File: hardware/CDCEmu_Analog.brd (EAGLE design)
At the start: 60 x 40 mm, 63 parts, among them J1 Audio In, J2 Audio Out, J3 Mic In, Q1 PCH, Q2 NCH, Q3 NCH, Q4 PCH, Q5 NCH, Q6 NPN, Q7 NPN, Q8 NPN, Q9 NPN, U1 1117, U2 BK8000L, U3 NE5532D

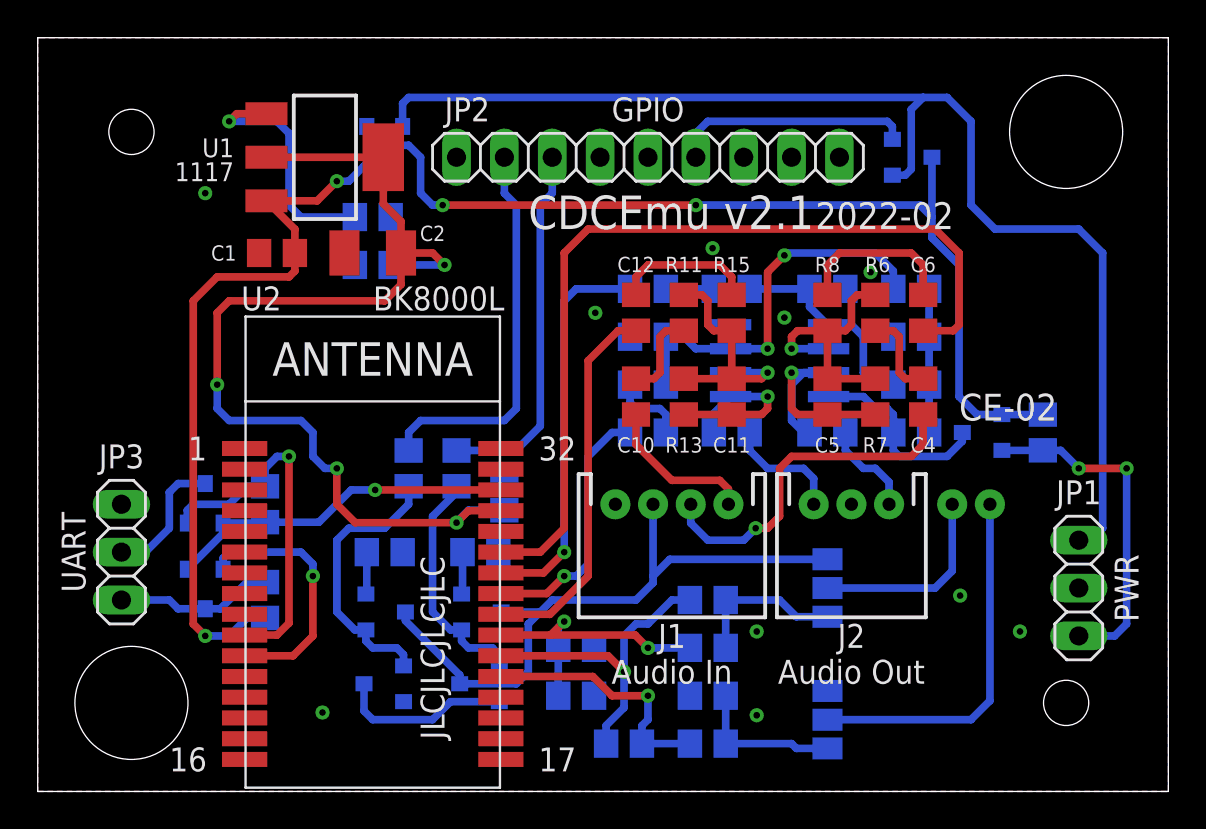
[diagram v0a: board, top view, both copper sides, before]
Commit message: [HW] Add audio gain control trimpots
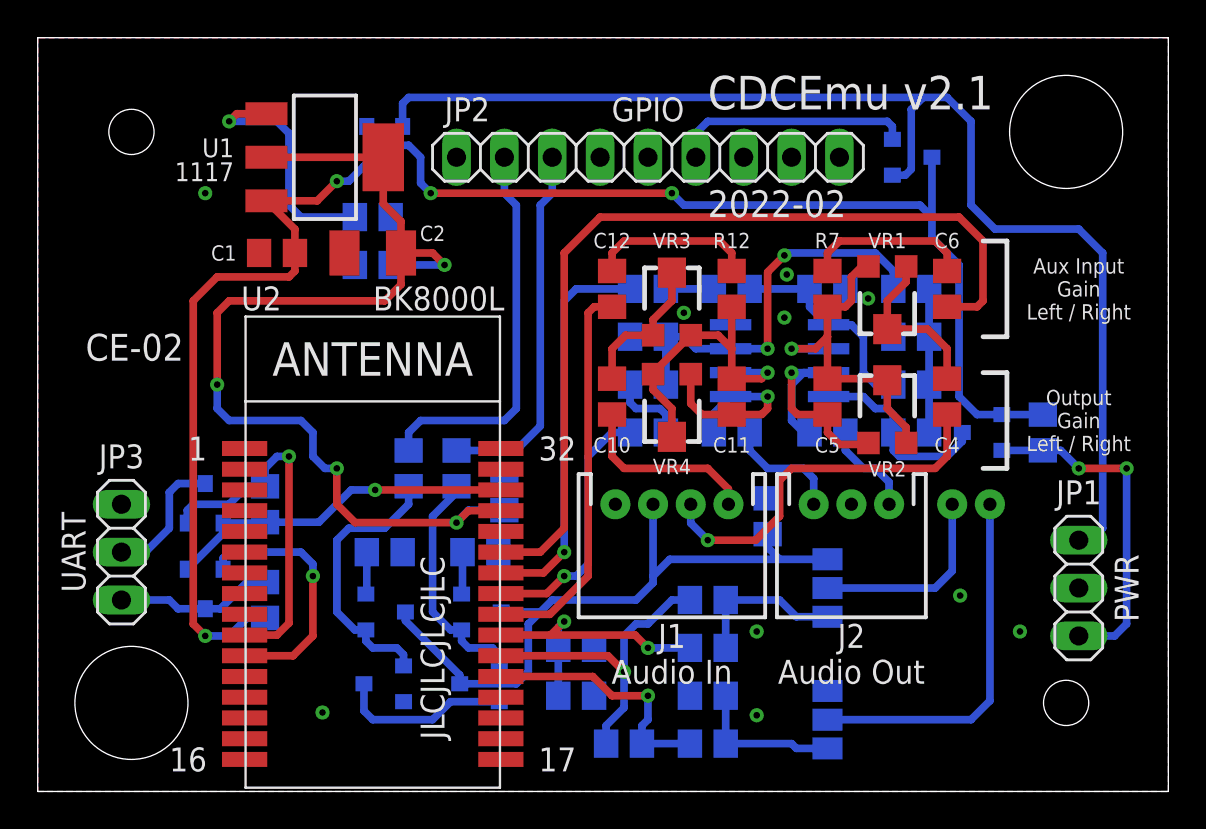
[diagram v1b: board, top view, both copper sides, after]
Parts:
- removed C16: 1u, rcl:C0805
- removed R21: 1k, rcl:R0805
- removed R22, R23: 1.2k, rcl:R0805
- added C21: 1u, rcl:C0805
- added VR1, VR2, VR3, VR4: 10k, SparkFun-Resistors:TRIMPOT-SMD-TC33X
- C17: value 10n -> 1u
- C18: value 1u -> 10n
- C19: value 100n -> 1u
- C20: value 1u -> 100n
- R10: value 1k -> 10k
- R18, R9: value 10k -> 1k
- R19, R20: value 10k -> 1.2k
- R6: value 10k -> 100k
- moved R18 31.2 mm to (46.4, 26.7)
- moved R17 25.6 mm to (46.4, 24.1), turned to 180 degrees
- moved R10 24.5 mm to (22.2, 17.1), turned to 270 degrees
- moved R14 23.7 mm to (23.5, 12.7)
- moved R15 22.4 mm to (18.4, 12.7), flipped to the bottom, turned to 0 degrees
- moved R20 21.9 mm to (35.6, 5.08)
- moved R12 17.4 mm to (36.8, 26.7), flipped to the top
- moved R13 15.1 mm to (19.7, 17.1), flipped to the bottom
- moved R19 14.3 mm to (35.6, 7.62)
- moved R11 13.6 mm to (46.4, 19.1), flipped to the bottom, turned to 0 degrees
- moved R16 13.5 mm to (32.4, 21.6), turned to 180 degrees
- moved R6 12.2 mm to (38.7, 14.6), flipped to the bottom, turned to 270 degrees
- moved R9 10.8 mm to (46.4, 21.6), turned to 0 degrees
- moved C17 8.82 mm to (35.6, 10.2)
- moved C19 7.43 mm to (35.6, 2.54)
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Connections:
- net +12V: now also R11.2; no longer R14.2
- net AGND: now also R11.1, R17.2, R18.1, R9.1; no longer R10.1, R14.1, R20.2, R21.1
- net BT_MICN: now also C19.2, R20.2; no longer C18.2, R23.2
- net BT_MICP: now also C17.2, R19.2; no longer C16.2, R22.2
- net CTRL: now also R6.2
- net GND: now also C21.2, R14.1, R15.1, R6.1; no longer C19.2, R18.1, R23.1
- net L+: now also R16.2, R18.2; no longer R19.2, R21.2
- net L-: now also R12.2, VR3.3, VR4.2, VR4.3; no longer R11.2, R13.1, R15.2
- net L1: now also VR3.1, VR3.2; no longer R11.1
- net L2: now also R12.1; no longer R15.1
- net L3: now also R16.1; no longer R19.1
- net LOUT: now also VR4.1; no longer R13.2
- net MIC_N: now also C18.2, C19.1; no longer C17.2, C18.1
- net MIC_P: now also C18.1; no longer C16.1
- net P3: now also R10.1; no longer R12.1
- net P3B: now also R10.2; no longer R12.2
- net P7: now also R13.1; no longer R16.1
- net P7B: now also R13.2; no longer R16.2
- net Q7E: now also R14.2; no longer R17.2
- net Q8E: now also R15.2; no longer R18.2
- net R+: now also R8.2; no longer R10.2
- net R-: now also R7.2, VR1.3, VR2.2, VR2.3; no longer R6.2, R7.1, R8.2
- net R1: now also VR1.1, VR1.2; no longer R6.1
- net R2: now also R7.1; no longer R8.1
- net R3: now also R8.1; no longer R9.1
- net ROUT: now also VR2.1; no longer R7.2
- net VMIC: now also C21.1, R19.1; no longer C19.1, R22.1
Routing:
- net R-: track 13.8 -> 18.7 mm
- net R1: track 4.71 -> 8.93 mm
- net L-: track 13.2 -> 16.9 mm
- net L1: track 4.71 -> 7.80 mm
- net AUX_L: track 8.28 -> 9.93 mm
- net CTRL: track 34.8 -> 36.4 mm
- net LOUT: track 9.45 -> 10.9 mm
- net L2: track 7.52 -> 8.79 mm
- net AUX_R: track 18.9 -> 20.2 mm
- net BT_RN: track 46.3 -> 47.2 mm
- net ROUT: track 13.8 -> 14.7 mm
- net BT_LN: track 20.1 -> 20.8 mm
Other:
- board text added: "Aux Input Gain Left / Right"
- board text added: "Mic Input Target"
- board text added: "Output Gain Left / Right"

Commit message: [HW/Analog] Add audio signal detection
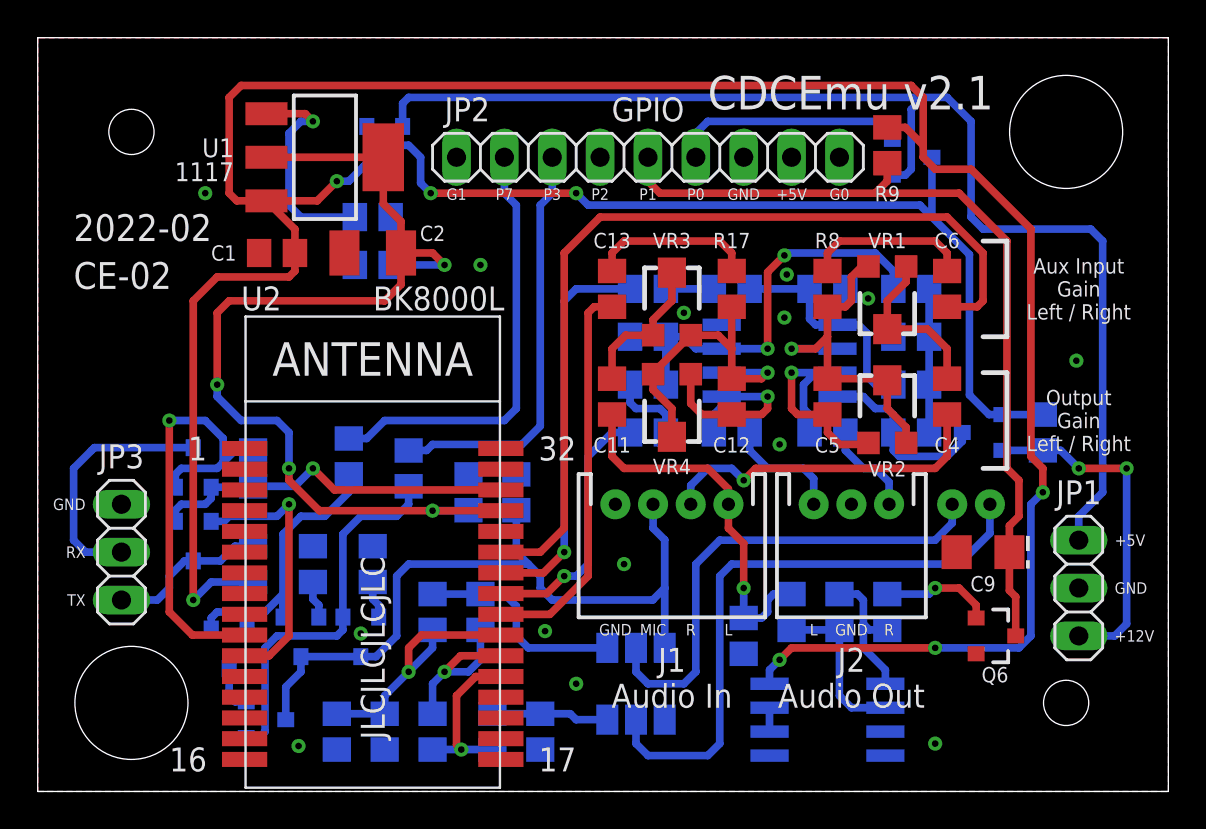
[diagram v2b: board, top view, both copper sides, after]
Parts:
- added C16: 47p, rcl:C0805
- added Q10: NPN, SparkFun-DiscreteSemi:SOT23-3
- added R21, R22: 10k, rcl:R0805
- added R23: 1k, rcl:R0805
- added R24, R25: 1.2k, rcl:R0805
- added U4: NE5532, custom:SO08
- C10, C12: value 1u -> 47p
- C11, C15: value 47p -> 1u
- C9: value 47p -> 10u; device rcl:C0805 -> custom:C1206-POL
- R11: value 10k -> 220
- R13: value 10k -> 1k
- R18: value 1k -> 10k
- R19, R20: value 1.2k -> 10k
- R6: value 100k -> 10k
- R7: value 10k -> 100k
- R9: value 1k -> 100k
- U3: value NE5532D -> LM358; device linear:SO08 -> custom:SO08
- moved R18 31.1 mm to (16.5, 17.8), turned to 270 degrees
- moved Q6 27.4 mm to (50.8, 8.26), flipped to the top
- moved R13 27.0 mm to (46.4, 21.6), turned to 0 degrees
- moved R20 22.1 mm to (14.6, 12.1), turned to 270 degrees
- moved R7 19.7 mm to (25.4, 15.9), flipped to the bottom
- moved U3 19.2 mm to (41.9, 3.81), turned to 270 degrees
- moved R12 19.0 mm to (45.1, 9.53), flipped to the bottom, turned to 90 degrees
- moved R19 18.3 mm to (17.8, 12.1), turned to 270 degrees
- moved R10 17.4 mm to (36.8, 26.7), turned to 180 degrees
- moved C9 16.2 mm to (50.2, 12.7), flipped to the top, turned to 180 degrees
- moved R14 14.7 mm to (37.5, 8.26), turned to 90 degrees
- moved R16 14.2 mm to (46.4, 19.1), turned to 0 degrees
- moved C21 13.5 mm to (15.9, 3.17), turned to 270 degrees
- moved Q7 12.8 mm to (12.1, 3.81)
- moved C10 12.8 mm to (41.9, 26.7), flipped to the bottom, turned to 0 degrees
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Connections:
- new net DET-: R11.2, R6.1, U3.2
- new net DETOUT: R12.1, R6.2, U3.1
- new net DET_B: Q6.1, R12.2
- new net U4FB: U3.6, U3.7
- net +12V: now also R16.2, U4.8; no longer R11.2, U3.8
- net +5V: now also R9.2, U3.8
- net AGND: now also R13.1, R16.1, R22.2, R23.1; no longer R11.1, R17.2, R18.1, R9.1
- net AUX_L: now also C11.1, R11.1, R14.2; no longer C10.1
- net BT_LN: now also C13.1; no longer C12.1
- net BT_LP: now also C15.1; no longer C14.1
- net BT_MICN: now also R25.2, SJ1.1; no longer R20.2, SJ1.3
- net BT_MICP: now also R24.2, SJ2.1; no longer R19.2, SJ2.3
- net CCE: now also Q10.3, Q7.2; no longer Q6.2, Q9.3
- net CTRL: now also Q9.3, R7.2, SJ2.3; no longer Q6.3, R6.2, SJ2.1
- net GND: now also C10.1, C16.1, C9.2, Q10.2, Q6.2, R19.1, R22.1, R25.1, R7.1, SJ1.3, U3.3, U3.5, U4.4; no longer C15.1, C9.1, Q9.2, R15.1, R17.1, R6.1, SJ1.1
- net L: now also C14.2; no longer C13.2
- net L+: now also C16.2, R21.2, R23.2, U4.3; no longer C15.2, R16.2, R18.2, U3.3
- net L-: now also C12.1, R17.2, U4.2; no longer C11.1, R12.2, U3.2
- net L1: now also C11.2; no longer C10.2
- net L2: now also C13.2, R17.1; no longer C12.2, R12.1
- net L3: now also C15.2, R21.1; no longer C14.2, R16.1
- net LOUT: now also C12.2, C14.1, U4.1; no longer C11.2, C13.1, U3.1
- net P1: now also C9.1, Q6.3, R9.1
- net P3: now also R15.1; no longer R10.1
- net P3B: now also Q8.1, R15.2; no longer Q6.1, R10.2
- net P7: now also R18.1; no longer R13.1
- net P7B: now also Q10.1, R18.2; no longer Q8.1, R13.2
- net Q7E: now also Q8.2, R19.2; no longer Q7.2, R14.2
- net Q8E: now also Q9.2, R20.2; no longer Q8.2, R15.2
- net R+: now also C10.2, R10.2, R13.2, U4.5; no longer C9.2, R8.2, R9.2, U3.5
- net R-: now also R8.2, U4.6; no longer R7.2, U3.6
- net R2: now also R8.1; no longer R7.1
- net R3: now also R10.1; no longer R8.1
- net ROUT: now also U4.7; no longer U3.7
- net VMIC: now also R24.1; no longer R19.1
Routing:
- net +5V: track 39.1 -> 131.7 mm, vias 2 -> 5
- net P1: track 0.00 -> 45.1 mm
- net MIC: track 10.5 -> 26.2 mm
- net MICGND: track 19.5 -> 31.9 mm
- net AUX_L: track 9.93 -> 19.7 mm, vias 0 -> 1
- net DET-: track 0.00 -> 8.74 mm
- net DETOUT: track 0.00 -> 7.73 mm
- net MIC_P: track 17.3 -> 9.59 mm
- net P3B: track 12.6 -> 20.3 mm
- net CCE: track 9.21 -> 2.48 mm
- net RX: track 7.07 -> 13.4 mm
- net DET_B: track 0.00 -> 5.91 mm, vias 0 -> 1
- net BT_RX: track 19.3 -> 24.5 mm
- net MIC_N: track 13.4 -> 8.91 mm
- net BT_MICP: track 8.31 -> 11.4 mm
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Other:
- board text added: "+"
- board text added: "+12V"
- board text added: "+5V"
- board text added: "-"
- board text added: "G0"
- board text added: "G1"
- board text added: "GND"
- board text added: "L"
- board text added: "MIC"
- board text added: "P0"
- board text added: "P1"
- board text added: "P2"
- board text added: "P3"
- board text added: "P7"
- board text added: "R"
- board text added: "RX"
- board text added: "TX"

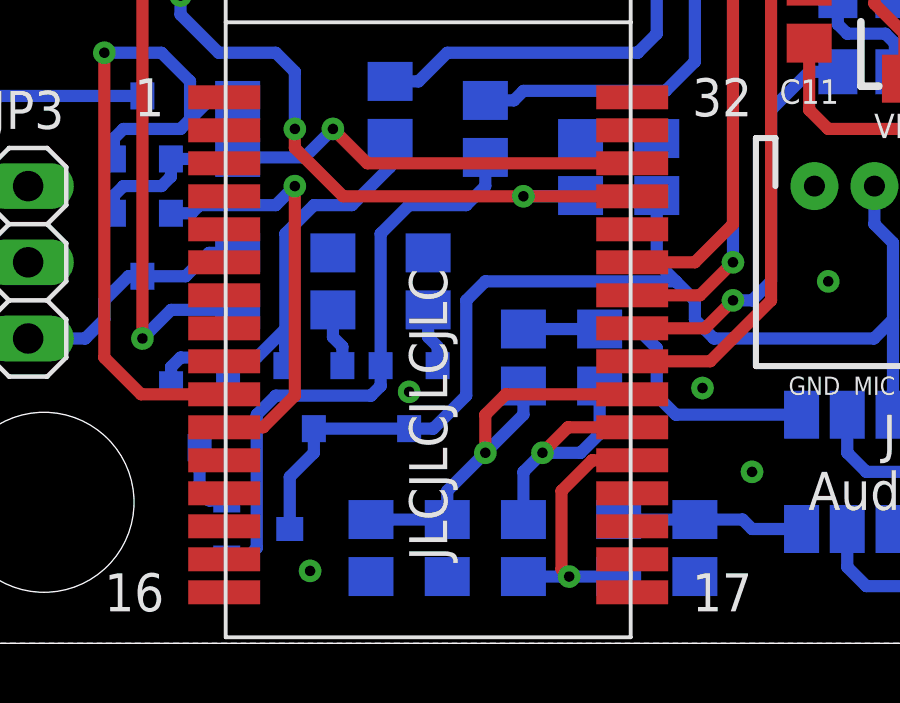
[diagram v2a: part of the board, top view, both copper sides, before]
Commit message: [HW/Analog] Separate Q8 and Q9
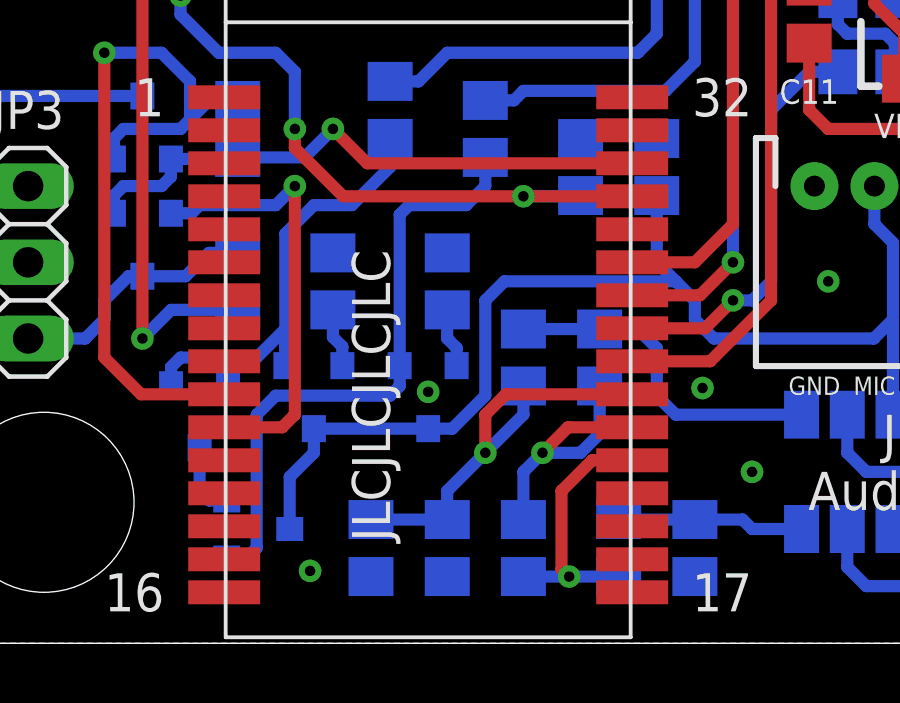
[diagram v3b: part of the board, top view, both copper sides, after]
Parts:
- moved Q8 0.64 mm to (17.8, 8.26)
- moved R19 0.63 mm to (18.4, 12.1)

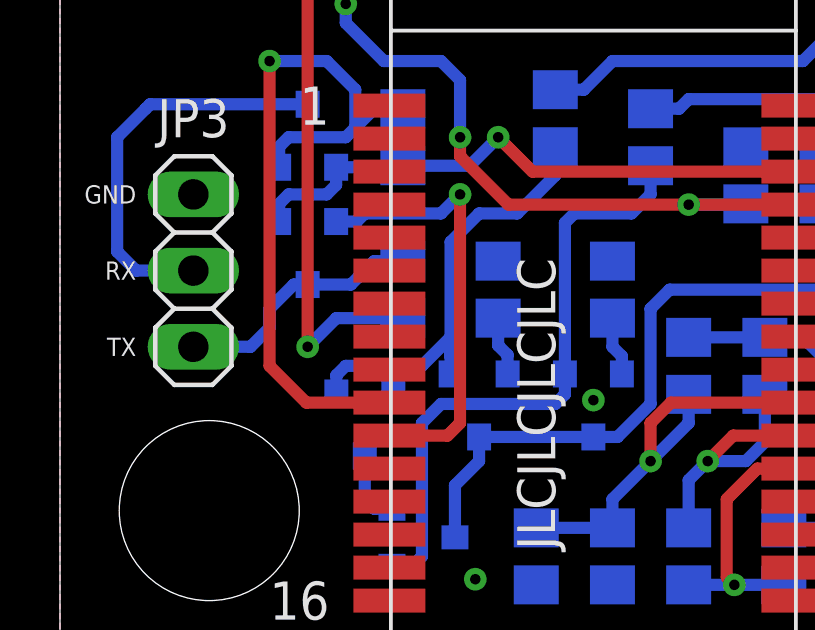
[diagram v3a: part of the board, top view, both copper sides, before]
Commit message: [HW/Analog] Fix swapped Bluetooth RX and TX
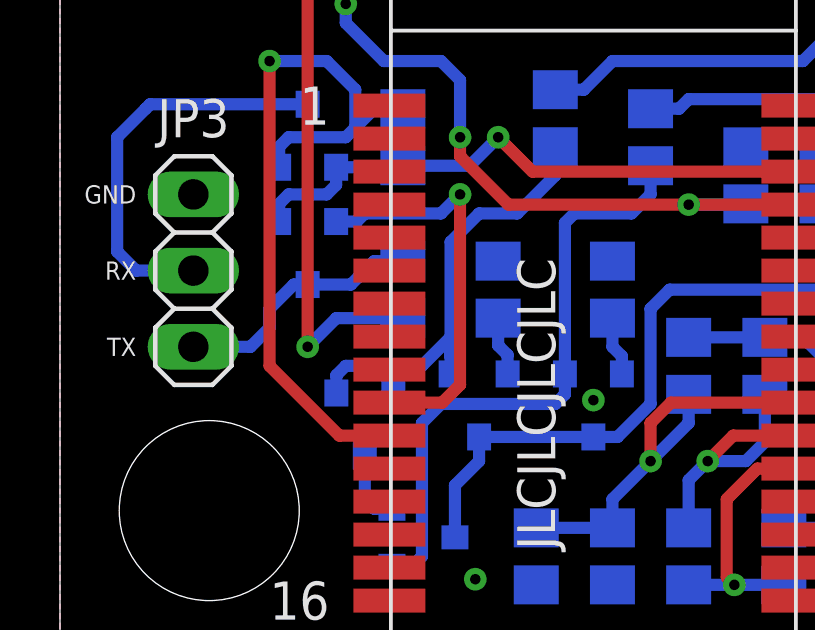
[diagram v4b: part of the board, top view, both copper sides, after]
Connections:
- net BT_RX: now also U2.11; no longer U2.10
- net BT_TX: now also U2.10; no longer U2.11
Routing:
- net BT_TX: track 14.7 -> 13.5 mm
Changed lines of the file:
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@@
 </signal>
 <signal name="BT_RX">
-<contactref element="U2" pad="10"/>
 <contactref element="R1" pad="1"/>
 <contactref element="Q2" pad="2"/>
-<wire x1="10.98" y1="8.3" x2="8.21" y2="8.3" width="0.4064" layer="1"/>
-<wire x1="8.21" y1="8.3" x2="6.985" y2="9.525" width="0.4064" layer="1"/>
 <wire x1="6.985" y1="9.525" x2="6.985" y2="19.685" width="0.4064" layer="1"/>
 <via x="6.985" y="19.685" extent="1-16" drill="0.35" shape="octagon"/>
@@
 <wire x1="9.8425" y1="18.7325" x2="9.8425" y2="17.4625" width="0.4064" layer="16"/>
 <wire x1="8.89" y1="19.685" x2="9.8425" y2="18.7325" width="0.4064" layer="16"/>
+<contactref element="U2" pad="11"/>
+<wire x1="10.98" y1="7.2" x2="9.31" y2="7.2" width="0.4064" layer="1"/>
+<wire x1="9.31" y1="7.2" x2="6.985" y2="9.525" width="0.4064" layer="1"/>
 </signal>
 <signal name="BT_TX">
 <contactref element="Q5" pad="2"/>
-<contactref element="U2" pad="11"/>
-<wire x1="12.915" y1="7.2" x2="13.335" y2="7.62" width="0.4064" layer="1"/>
 <wire x1="9.205" y1="14.335" x2="9.89" y2="14.335" width="0.4064" layer="16"/>
 <wire x1="9.89" y1="14.335" x2="10.16" y2="14.605" width="0.4064" layer="16"/>
 <wire x1="12.7" y1="14.605" x2="13.335" y2="15.24" width="0.4064" layer="16"/>
 <wire x1="12.7" y1="14.605" x2="10.16" y2="14.605" width="0.4064" layer="16"/>
-<wire x1="10.98" y1="7.2" x2="12.915" y2="7.2" width="0.4064" layer="1"/>
 <via x="13.335" y="15.24" extent="1-16" drill="0.35" shape="octagon"/>
-<wire x1="13.335" y1="7.62" x2="13.335" y2="15.24" width="0.4064" layer="1"/>
+<wire x1="13.335" y1="8.89" x2="13.335" y2="15.24" width="0.4064" layer="1"/>
+<contactref element="U2" pad="10"/>
+<wire x1="10.98" y1="8.3" x2="12.745" y2="8.3" width="0.4064" layer="1"/>
+<wire x1="12.745" y1="8.3" x2="13.335" y2="8.89" width="0.4064" layer="1"/>
 </signal>
 <signal name="+3V3">
